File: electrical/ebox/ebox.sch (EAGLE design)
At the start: 20 parts, among them IC1 MAX3221CUE, U1 AT32UC3C1512/1256/1128, X1 22-23-2031, X2 22-23-2031, X3 C-GRID-07-70543, X4 22-23-2021, X5 C-GRID-07-70543, X6 C-GRID-07-70543, X7 C-GRID-07-70543, X8 C-GRID-07-70543, X9 C-GRID-07-70543

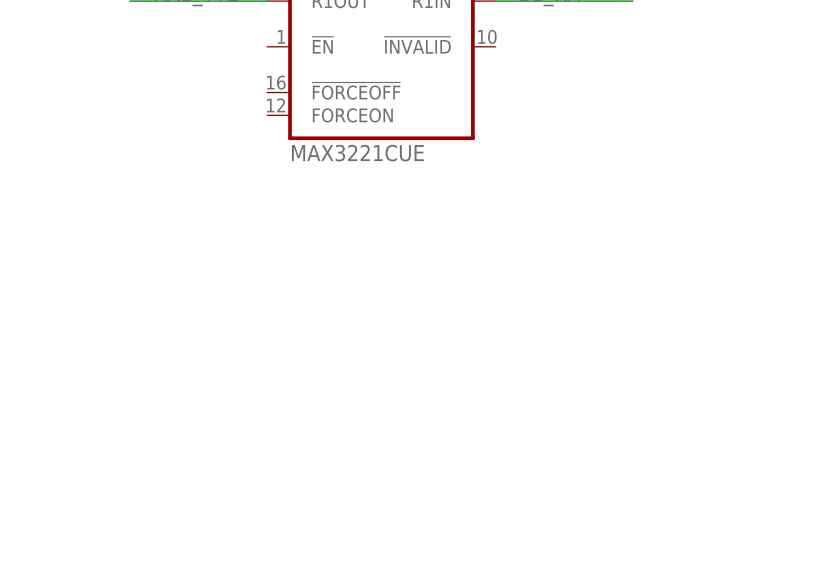
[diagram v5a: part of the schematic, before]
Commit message: Added ext volt reg.
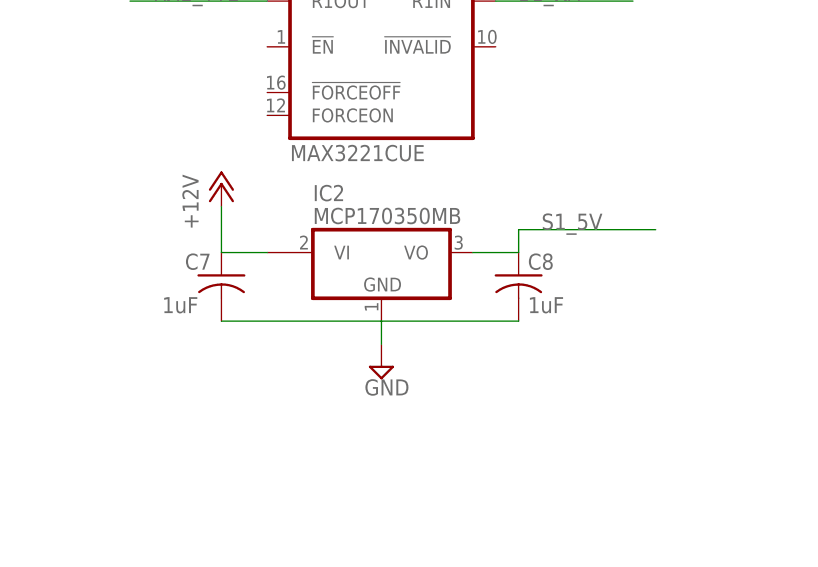
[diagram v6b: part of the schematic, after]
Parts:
- added C7, C8: 1uF, rcl:C-USC0805
- added IC2: MCP170350MB, linear:MCP170350MB
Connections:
- new net +12V: C7.1, IC2.VI1
- net GND: now also C7.2, C8.2, IC2.GND
- net S1_5V: now also C8.1, IC2.VO
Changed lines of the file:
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@@
 <part name="SUPPLY2" library="supply2" deviceset="GND" device=""/>
 <part name="+3V1" library="supply1" deviceset="+3V3" device=""/>
+<part name="IC2" library="linear" deviceset="MCP1703*" device="MB" technology="50"/>
+<part name="C8" library="rcl" deviceset="C-US" device="C0805" value="1uF"/>
+<part name="C7" library="rcl" deviceset="C-US" device="C0805" value="1uF"/>
+<part name="SUPPLY3" library="supply2" deviceset="GND" device=""/>
+<part name="P+1" library="supply1" deviceset="+12V" device=""/>
 </parts>
 <sheets>
@@
 <instance part="SUPPLY2" gate="GND" x="220.98" y="210.82"/>
 <instance part="+3V1" gate="G$1" x="220.98" y="233.68"/>
+<instance part="IC2" gate="G$1" x="259.08" y="175.26"/>
+<instance part="C8" gate="G$1" x="274.32" y="172.72"/>
+<instance part="C7" gate="G$1" x="241.3" y="172.72" smashed="yes">
+<attribute name="NAME" x="237.236" y="173.355" size="1.778" layer="95"/>
+<attribute name="VALUE" x="234.696" y="168.529" size="1.778" layer="96"/>
+</instance>
+<instance part="SUPPLY3" gate="GND" x="259.08" y="162.56"/>
+<instance part="P+1" gate="1" x="241.3" y="182.88"/>
 </instances>
 <busses>
@@
 <junction x="220.98" y="213.36"/>
 </segment>
+<segment>
+<pinref part="C7" gate="G$1" pin="2"/>
+<pinref part="IC2" gate="G$1" pin="GND"/>
+<wire x1="241.3" y1="167.64" x2="259.08" y2="167.64" width="0.1524" layer="91"/>
+<pinref part="C8" gate="G$1" pin="2"/>
+<wire x1="259.08" y1="167.64" x2="274.32" y2="167.64" width="0.1524" layer="91"/>
+<pinref part="SUPPLY3" gate="GND" pin="GND"/>
+<wire x1="259.08" y1="167.64" x2="259.08" y2="165.1" width="0.1524" layer="91"/>
+</segment>
 </net>
 <net name="S1_12V" class="0">
@@
 <wire x1="365.76" y1="195.58" x2="350.52" y2="195.58" width="0.1524" layer="91"/>
 <label x="353.06" y="195.58" size="1.778" layer="95"/>
+</segment>
+<segment>
+<pinref part="IC2" gate="G$1" pin="VO"/>
+<pinref part="C8" gate="G$1" pin="1"/>
+<wire x1="269.24" y1="175.26" x2="274.32" y2="175.26" width="0.1524" layer="91"/>
+<wire x1="274.32" y1="175.26" x2="274.32" y2="177.8" width="0.1524" layer="91"/>
+<wire x1="274.32" y1="177.8" x2="289.56" y2="177.8" width="0.1524" layer="91"/>
+<label x="276.86" y="177.8" size="1.778" layer="95"/>
 </segment>
 </net>
@@
 </segment>
 </net>
+<net name="+12V" class="0">
+<segment>
+<pinref part="C7" gate="G$1" pin="1"/>
+<pinref part="IC2" gate="G$1" pin="VI1"/>
+<wire x1="241.3" y1="175.26" x2="246.38" y2="175.26" width="0.1524" layer="91"/>
+<wire x1="241.3" y1="175.26" x2="241.3" y2="180.34" width="0.1524" layer="91"/>
+<pinref part="P+1" gate="1" pin="+12V"/>
+</segment>
+</net>

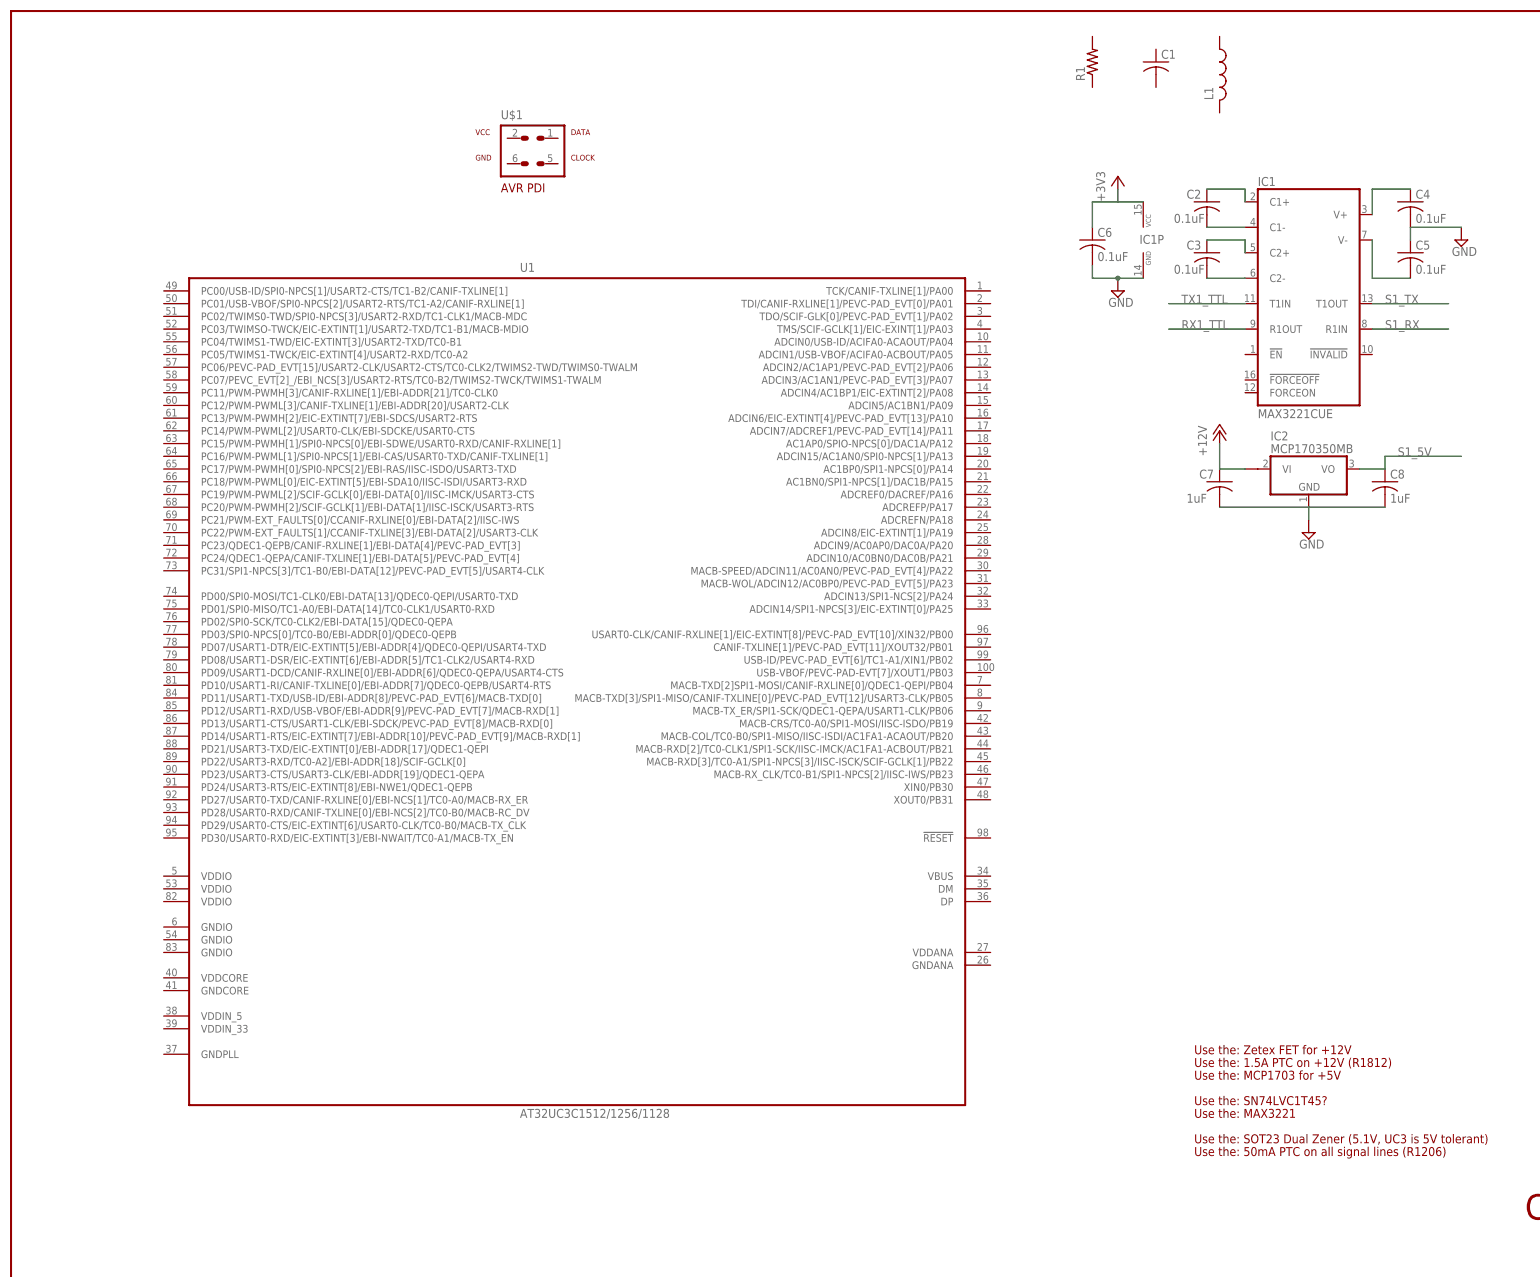
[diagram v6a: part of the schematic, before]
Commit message: Finished all the avr boilerplate.
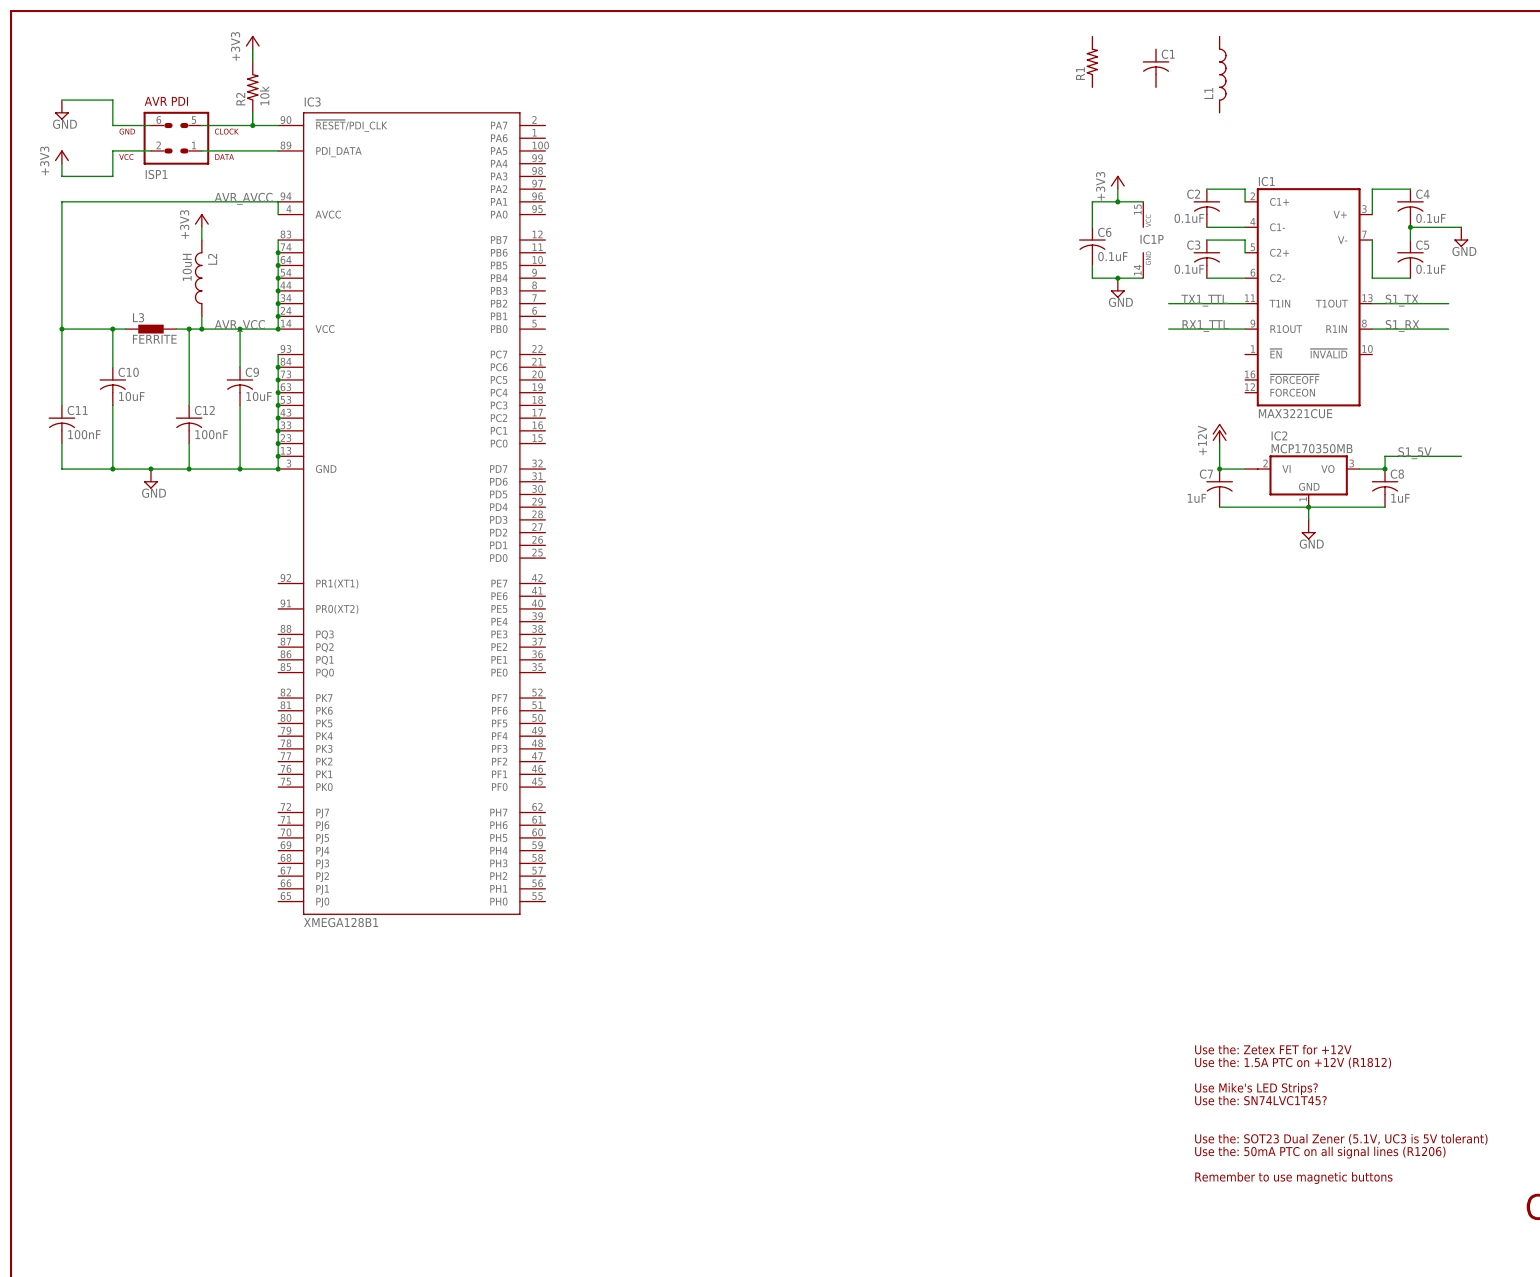
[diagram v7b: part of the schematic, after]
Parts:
- removed U$1: AVR-PDIVERT, avr-7:AVR-PDIVERT
- removed U1: AT32UC3C1512/1256/1128, atmel-avr32-michel:AT32UC3C1512/1256/1128
- added C10, C9: 10uF, rcl:C-USC0805
- added C11, C12: 100nF, rcl:C-USC0805
- added IC3: XMEGA128B1, atmel:XMEGA128A1
- added ISP1: AVR-PDIVERT, avr-7:AVR-PDIVERT
- added L2: 10uH, rcl:L-USL2012C
- added L3: FERRITE, inductors:BML15HB121SN1
- added R2: 10k, rcl:R-US_R0805
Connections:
- new net AVR_AVCC: C10.1, C11.1, IC3.AVCC, IC3.AVCC1, L3.1
- new net AVR_VCC: C12.1, C9.1, IC3.VCC, IC3.VCC1, IC3.VCC2, IC3.VCC3, IC3.VCC4, IC3.VCC5, IC3.VCC6, IC3.VCC7, L2.1, L3.2
- new net N$5: IC3.!RESET!/PDI_CLK, ISP1.5, R2.1
- new net N$7: IC3.PDI_DATA, ISP1.1
- net +3V3: now also ISP1.2, L2.2, R2.2
- net GND: now also C10.2, C11.2, C12.2, C9.2, IC3.GND, IC3.GND1, IC3.GND2, IC3.GND3, IC3.GND4, IC3.GND5, IC3.GND6, IC3.GND7, IC3.GND8, IC3.GND9, ISP1.6
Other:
- note added: "Remember to use magnetic buttons"
- note added: "Use Mike's LED Strips?"
- note removed: "Use the: MAX3221"
- note removed: "Use the: MCP1703 for +5V"

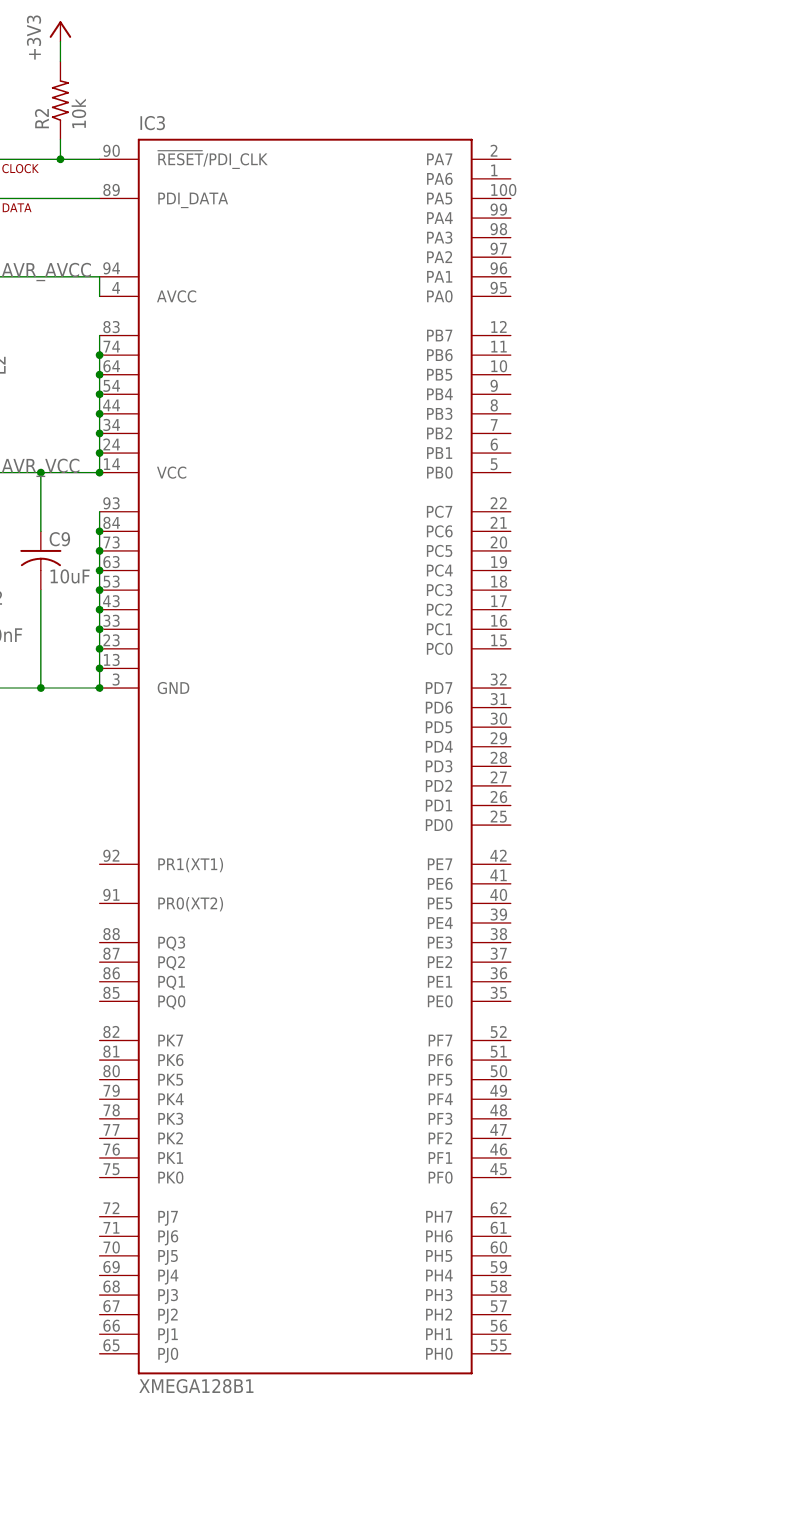
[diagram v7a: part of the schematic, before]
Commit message: Added most of the basic IO lines.
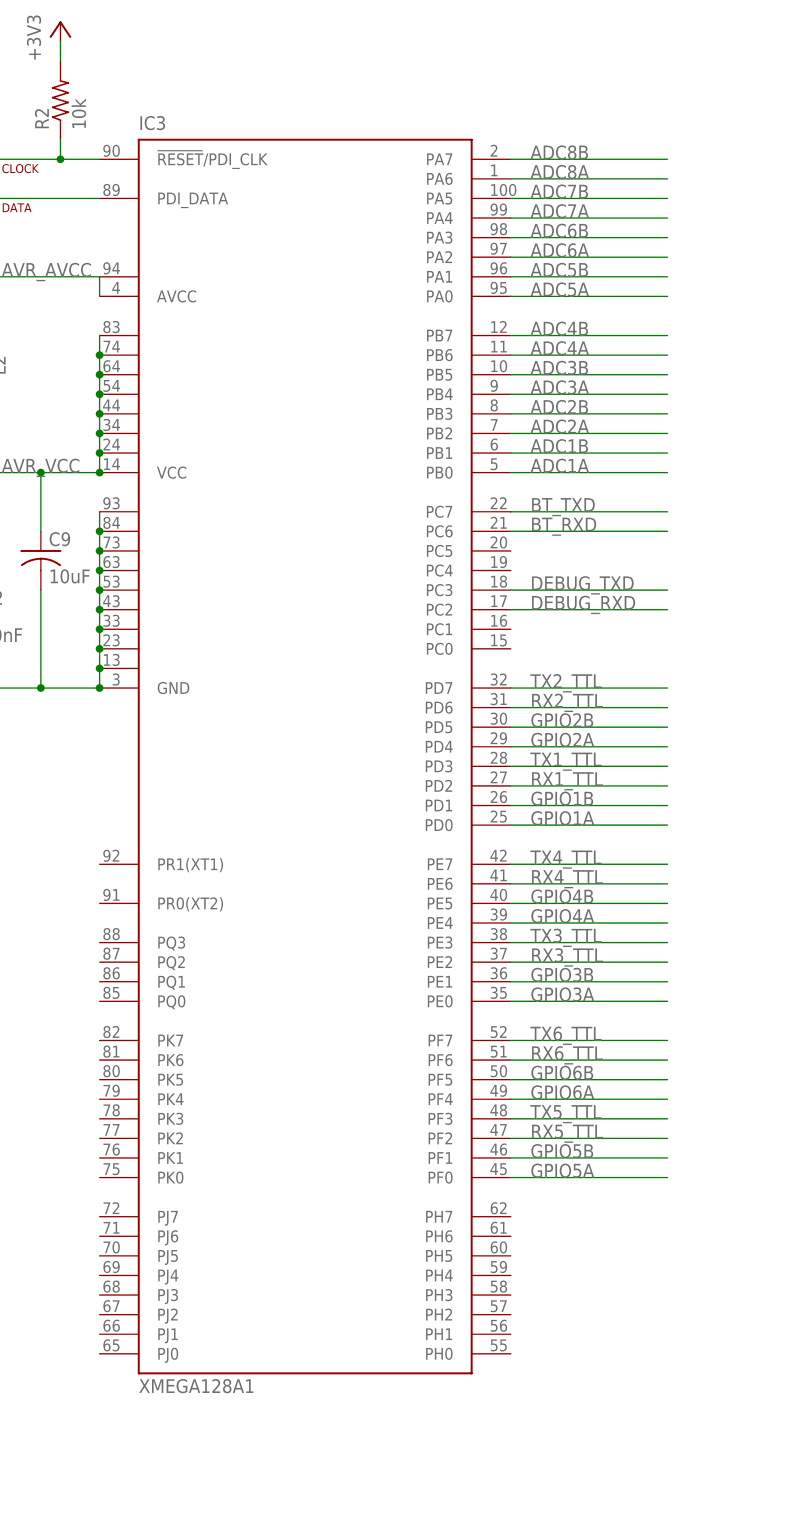
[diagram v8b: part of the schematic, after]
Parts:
- IC3: value XMEGA128B1 -> XMEGA128A1
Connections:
- new net ADC1A: IC3.PB0
- new net ADC1B: IC3.PB1
- new net ADC2A: IC3.PB2
- new net ADC2B: IC3.PB3
- new net ADC3A: IC3.PB4
- new net ADC3B: IC3.PB5
- new net ADC4A: IC3.PB6
- new net ADC4B: IC3.PB7
- new net ADC5A: IC3.PA0
- new net ADC5B: IC3.PA1
- new net ADC6A: IC3.PA2
- new net ADC6B: IC3.PA3
- new net ADC7A: IC3.PA4
- new net ADC7B: IC3.PA5
- new net ADC8A: IC3.PA6
- new net ADC8B: IC3.PA7
- new net BT_RXD: IC3.PC6
- new net BT_TXD: IC3.PC7
- new net DEBUG_RXD: IC3.PC2
- new net DEBUG_TXD: IC3.PC3
- new net GPIO1A: IC3.PD0
- new net GPIO1B: IC3.PD1
- new net GPIO2A: IC3.PD4
- new net GPIO2B: IC3.PD5
- new net GPIO3A: IC3.PE0
- new net GPIO3B: IC3.PE1
- new net GPIO4A: IC3.PE4
- new net GPIO4B: IC3.PE5
- new net GPIO5A: IC3.PF0
- new net GPIO5B: IC3.PF1
- new net GPIO6A: IC3.PF4
- new net GPIO6B: IC3.PF5
- new net RX2_TTL: IC3.PD6
- new net RX3_TTL: IC3.PE2
- new net RX4_TTL: IC3.PE6
- new net RX5_TTL: IC3.PF2
- new net RX6_TTL: IC3.PF6
- new net TX2_TTL: IC3.PD7
- new net TX3_TTL: IC3.PE3
- new net TX4_TTL: IC3.PE7
- new net TX5_TTL: IC3.PF3
- new net TX6_TTL: IC3.PF7
- net RX1_TTL: now also IC3.PD2
- net TX1_TTL: now also IC3.PD3
